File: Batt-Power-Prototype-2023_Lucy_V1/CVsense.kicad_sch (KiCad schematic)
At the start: 26 parts, among them U11 TSV912IDT, U5 ACS723xLCTR-10AU, U6 TSV912IDT, U8 TSV912IDT

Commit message: made changes to schematic
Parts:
- added C16 (x3): 100n, Capacitor_SMD:C_0603_1608Metric, symbol Device:C
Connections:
- net +5V: now also C16.1, C16.1, C16.1
- net GND: now also C16.2, C16.2, C16.2
- net Battery_Current renamed BAttery_Crrnt
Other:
- moved on the sheet: C16, U11C, U8C

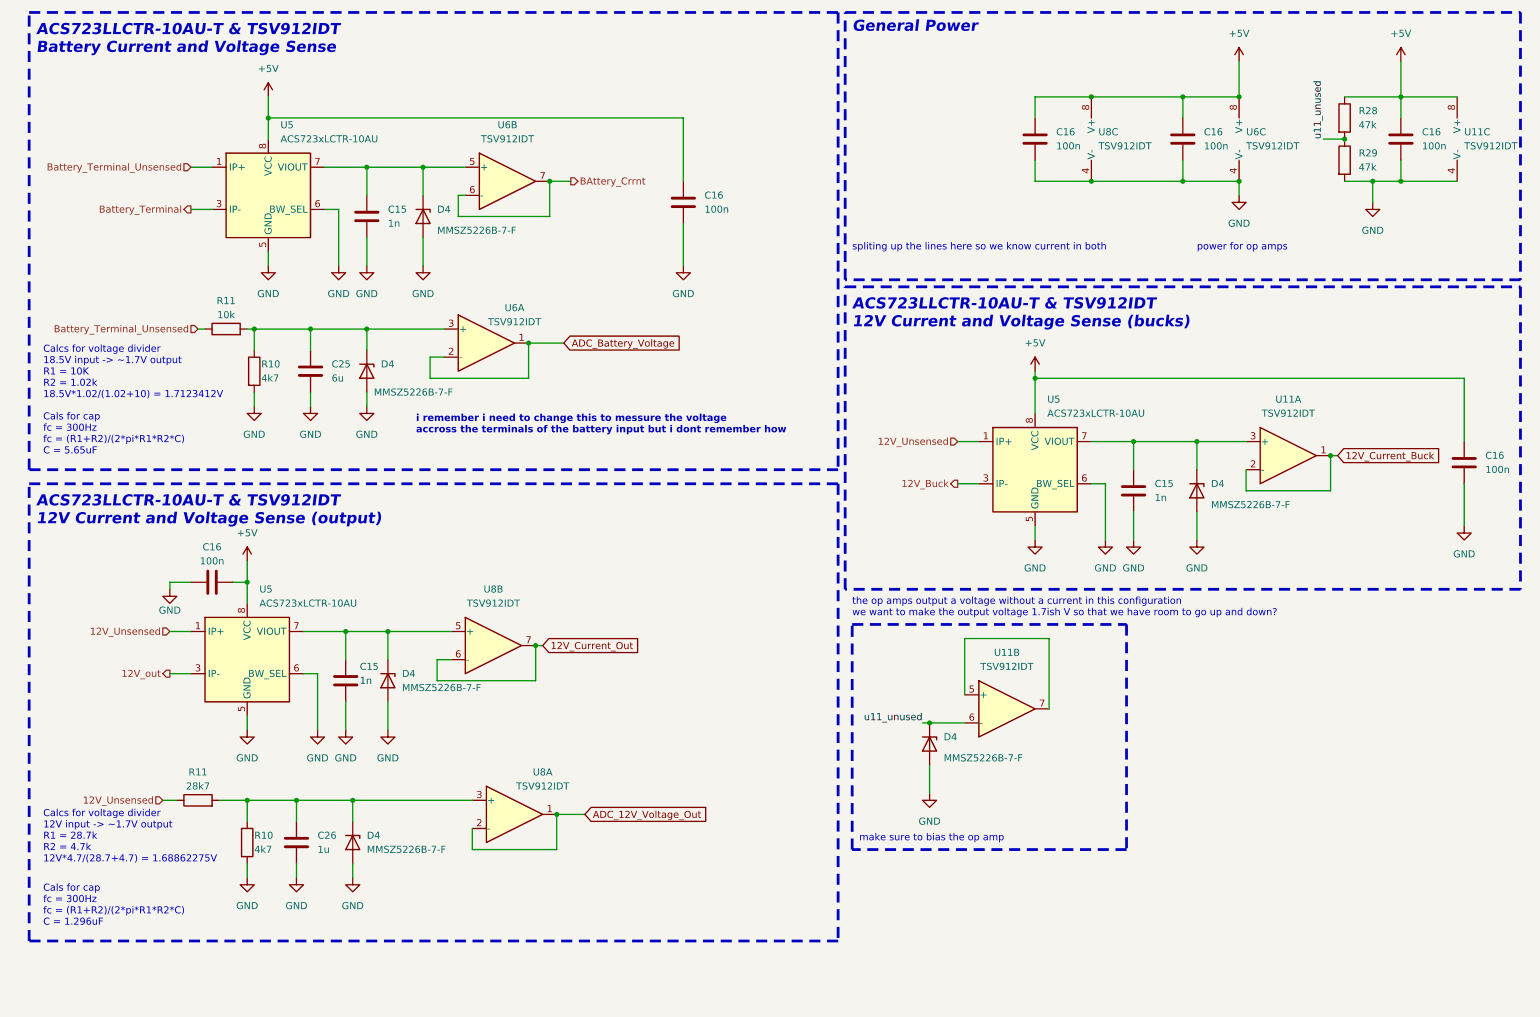
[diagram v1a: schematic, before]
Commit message: no more global variables
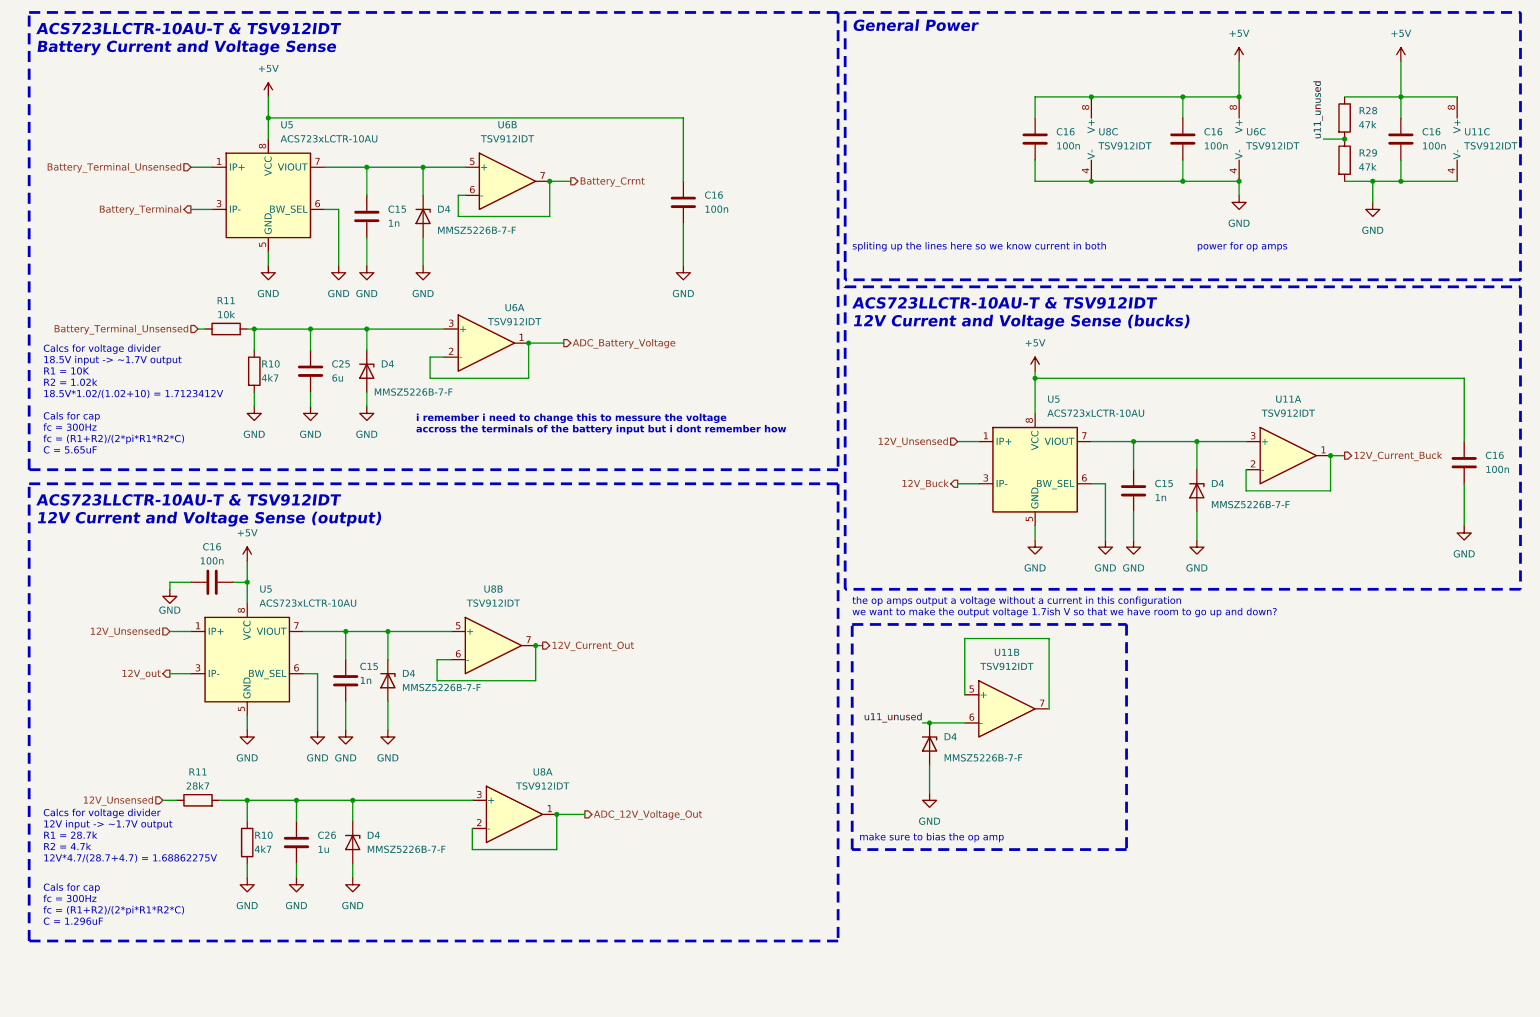
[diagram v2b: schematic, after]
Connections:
- net BAttery_Crrnt renamed Battery_Crrnt
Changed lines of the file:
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@@
     (stroke (width 0) (type default))
   )
-  (wire (pts (xy 248.92 93.98) (xy 250.19 93.98))
+  (wire (pts (xy 248.92 93.98) (xy 251.46 93.98))
     (stroke (width 0) (type default))
   )
@@
     (effects (font (size 1.27 1.27)) (justify right bottom))
   )
-  (global_label "12V_Current_Out" (shape input) (at 106.68 128.27 0) (fields_autoplaced)
-    (effects (font (size 1.27 1.27)) (justify left))
-    (property "Intersheetrefs" "${INTERSHEET_REFS}" (at 125.2679 128.27 0)
-      (effects (font (size 1.27 1.27)) (justify left) hide)
-    )
-  )
-  (global_label "12V_Current_Buck" (shape input) (at 250.19 93.98 0) (fields_autoplaced)
-    (effects (font (size 1.27 1.27)) (justify left))
-    (property "Intersheetrefs" "${INTERSHEET_REFS}" (at 270.1084 93.98 0)
-      (effects (font (size 1.27 1.27)) (justify left) hide)
-    )
-  )
-  (global_label "ADC_Battery_Voltage" (shape input) (at 110.49 73.66 0) (fields_autoplaced)
-    (effects (font (size 1.27 1.27)) (justify left))
-    (property "Intersheetrefs" "${INTERSHEET_REFS}" (at 132.7669 73.66 0)
-      (effects (font (size 1.27 1.27)) (justify left) hide)
-    )
-  )
-  (global_label "ADC_12V_Voltage_Out" (shape input) (at 114.3 158.75 0) (fields_autoplaced)
-    (effects (font (size 1.27 1.27)) (justify left))
-    (property "Intersheetrefs" "${INTERSHEET_REFS}" (at 137.5445 158.75 0)
-      (effects (font (size 1.27 1.27)) (justify left) hide)
-    )
-  )
   (hierarchical_label "Battery_Terminal_Unsensed" (shape input) (at 44.45 71.12 180) (fields_autoplaced)
     (effects (font (size 1.27 1.27)) (justify right))
@@
     (effects (font (size 1.27 1.27)) (justify right))
   )
+  (hierarchical_label "ADC_12V_Voltage_Out" (shape output) (at 114.3 158.75 0) (fields_autoplaced)
+    (effects (font (size 1.27 1.27)) (justify left))
+  )
+  (hierarchical_label "ADC_Battery_Voltage" (shape output) (at 110.49 73.66 0) (fields_autoplaced)
+    (effects (font (size 1.27 1.27)) (justify left))
+  )
   (hierarchical_label "12V_Unsensed" (shape input) (at 181.61 91.44 180) (fields_autoplaced)
     (effects (font (size 1.27 1.27)) (justify right))
@@
     (effects (font (size 1.27 1.27)) (justify right))
   )
-  (hierarchical_label "BAttery_Crrnt" (shape output) (at 111.76 44.45 0) (fields_autoplaced)
+  (hierarchical_label "Battery_Crrnt" (shape output) (at 111.76 44.45 0) (fields_autoplaced)
+    (effects (font (size 1.27 1.27)) (justify left))
+  )
+  (hierarchical_label "12V_Current_Out" (shape output) (at 106.68 128.27 0) (fields_autoplaced)
     (effects (font (size 1.27 1.27)) (justify left))
   )
@@
     (effects (font (size 1.27 1.27)) (justify right))
   )
+  (hierarchical_label "12V_Current_Buck" (shape output) (at 251.46 93.98 0) (fields_autoplaced)
+    (effects (font (size 1.27 1.27)) (justify left))
+  )
   (hierarchical_label "Battery_Terminal_Unsensed" (shape input) (at 43.18 41.91 180) (fields_autoplaced)

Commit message: some of the touch ups
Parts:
- removed C16 (x2): 100n, Capacitor_SMD:C_0603_1608Metric, symbol Device:C
- added C? (x2): 100n, Capacitor_SMD:C_0603_1608Metric, symbol Device:C
- renumbered C26 to C36, C25 to C37, C16 to C?, C15 to C?, D4 to D?, R28 to R29, R29 to R30, R10 to R?, R11 to R?, U6 to U13, U8 to U13, U6 to U14, U8 to U14, U11 to U15, U5 to U?
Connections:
- net +5V: now also C?.2, C?.2
- net GND: now also C?.1, C?.1
- net 12V_out renamed 12V_PCBs

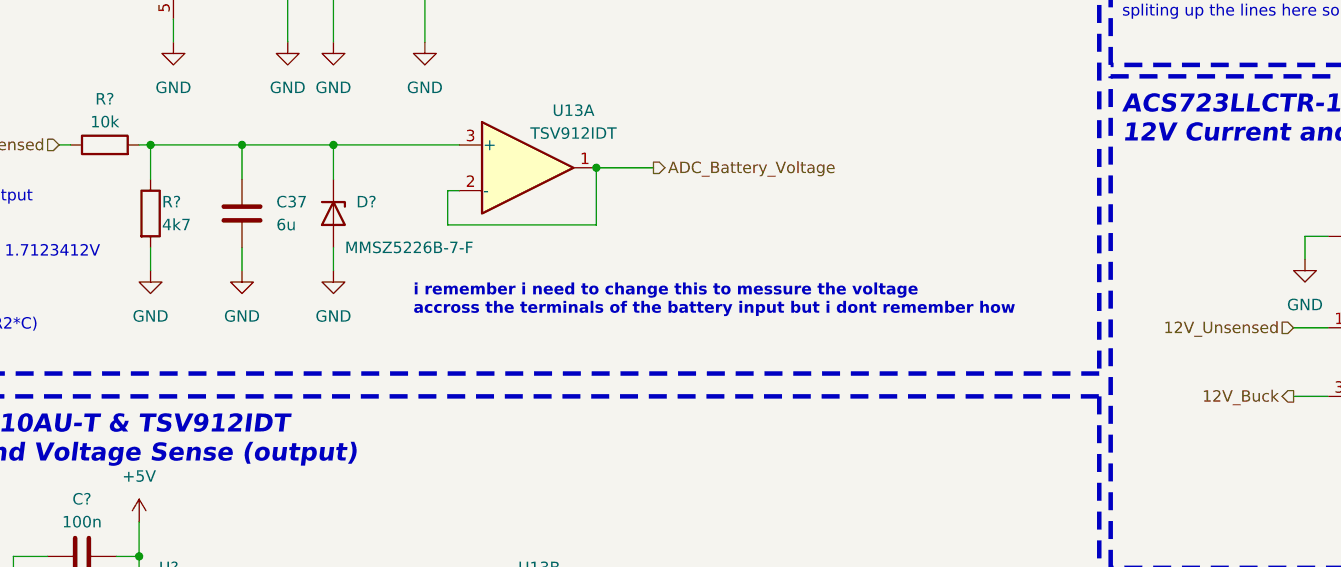
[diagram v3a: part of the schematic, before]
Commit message: everything but the battery input done
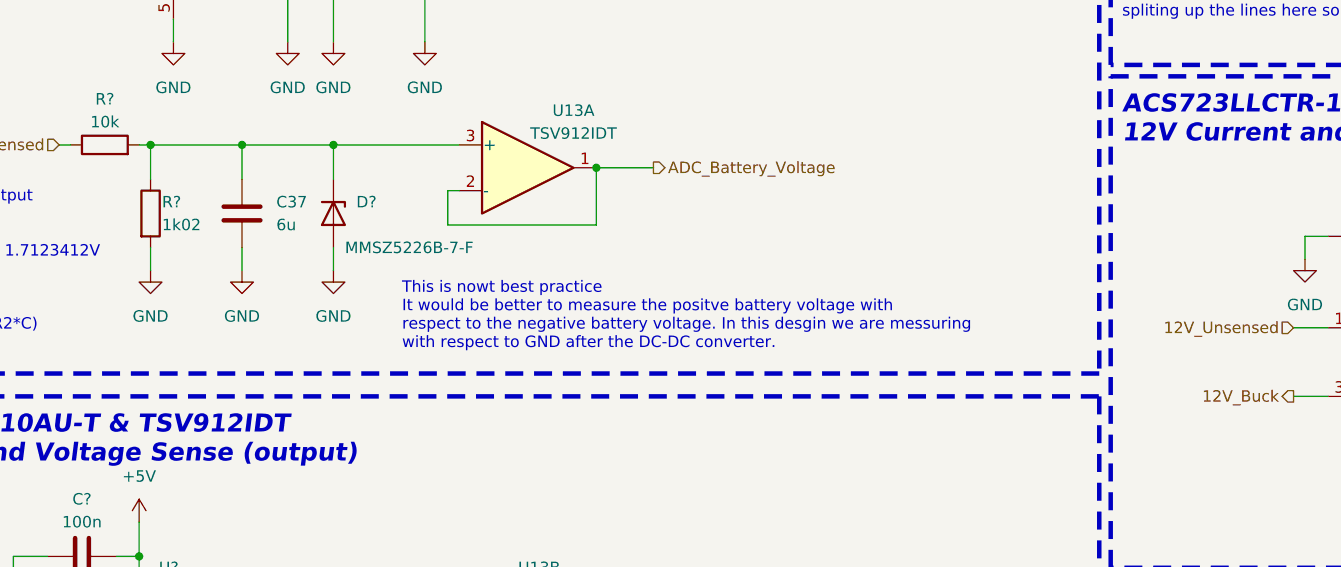
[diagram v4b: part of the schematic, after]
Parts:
- R?: value 4k7 -> 1k02
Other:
- note added: "This is nowt best practice It would be better to measure the positve battery voltage with respect to the negative battery voltage. In this desgin we are messuring with respect to GND after the DC-DC converter."
- note removed: "i remember i need to change this to messure the voltage accross the terminals of the battery input but i dont remember how"
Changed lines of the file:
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@@
     (effects (font (size 2 2) (thickness 0.254) bold italic) (justify left bottom))
+  )
+  (text "This is nowt best practice\nIt would be better to measure the positve battery voltage with \nrespect to the negative battery voltage. In this desgin we are messuring\nwith respect to GND after the DC-DC converter."
+    (at 82.55 93.98 0)
+    (effects (font (size 1.27 1.27)) (justify left bottom))
   )
   (text "Calcs for voltage divider\n18.5V input -> ~1.7V output\nR1 = 10K \nR2 = 1.02k\n18.5V*1.02/(1.02+10) = 1.7123412V"
@@
     (at 162.56 71.12 0)
     (effects (font (size 2 2) (thickness 0.254) bold italic) (justify left bottom))
-  )
-  (text "i remember i need to change this to messure the voltage \naccross the terminals of the battery input but i dont remember how"
-    (at 83.82 90.17 0)
-    (effects (font (size 1.27 1.27) (thickness 0.254) bold) (justify left bottom))
   )
   (text "spliting up the lines here so we know current in both\n"
@@
       (effects (font (size 1.27 1.27)) (justify left))
     )
-    (property "Value" "4k7" (at 55.88 80.01 0)
+    (property "Value" "1k02" (at 55.88 80.01 0)
       (effects (font (size 1.27 1.27)) (justify left))
     )

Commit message: everything
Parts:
- U13, U14, U15: Digikey # (none) -> 497-8165-2-ND
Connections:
- net 12V_Current_Out: now also U14.1, U14.2 (-); no longer U13.6 (-), U13.7
- net ADC_12V_Voltage_Out: now also U14.6 (-), U14.7; no longer U14.1, U14.2 (-)
- net ADC_Battery_Voltage: now also U13.6 (-), U13.7; no longer U13.1, U13.2 (-)
- net Battery_Crrnt: now also U13.1, U13.2 (-); no longer U14.6 (-), U14.7
- net at C37.1, D?.1 (K), R?.1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: now also U13.5 (+); no longer U13.3 (+)
- net at C?.1, D?.1 (K), U?.7 (VIOUT): now also U13.3 (+); no longer U14.5 (+)
- net at C?.1, D?.1 (K), U?.7 (VIOUT): now also U14.3 (+); no longer U13.5 (+)
- net at C36.1, D?.1 (K), R?.1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: now also U14.5 (+); no longer U14.3 (+)
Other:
- moved on the sheet: U13A, U13B, U14A, U14B

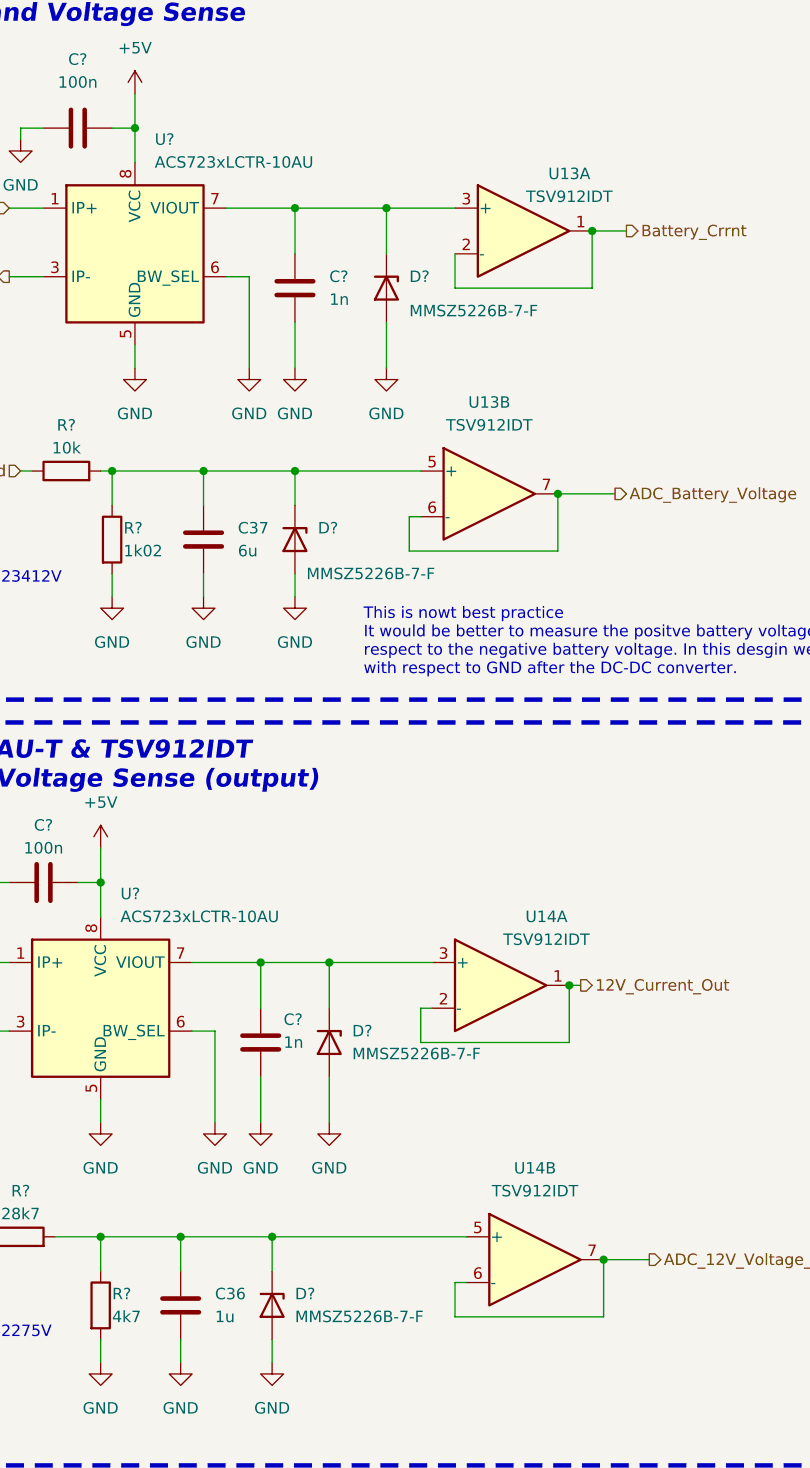
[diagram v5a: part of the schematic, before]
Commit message: Added bucks and fixed pinouts
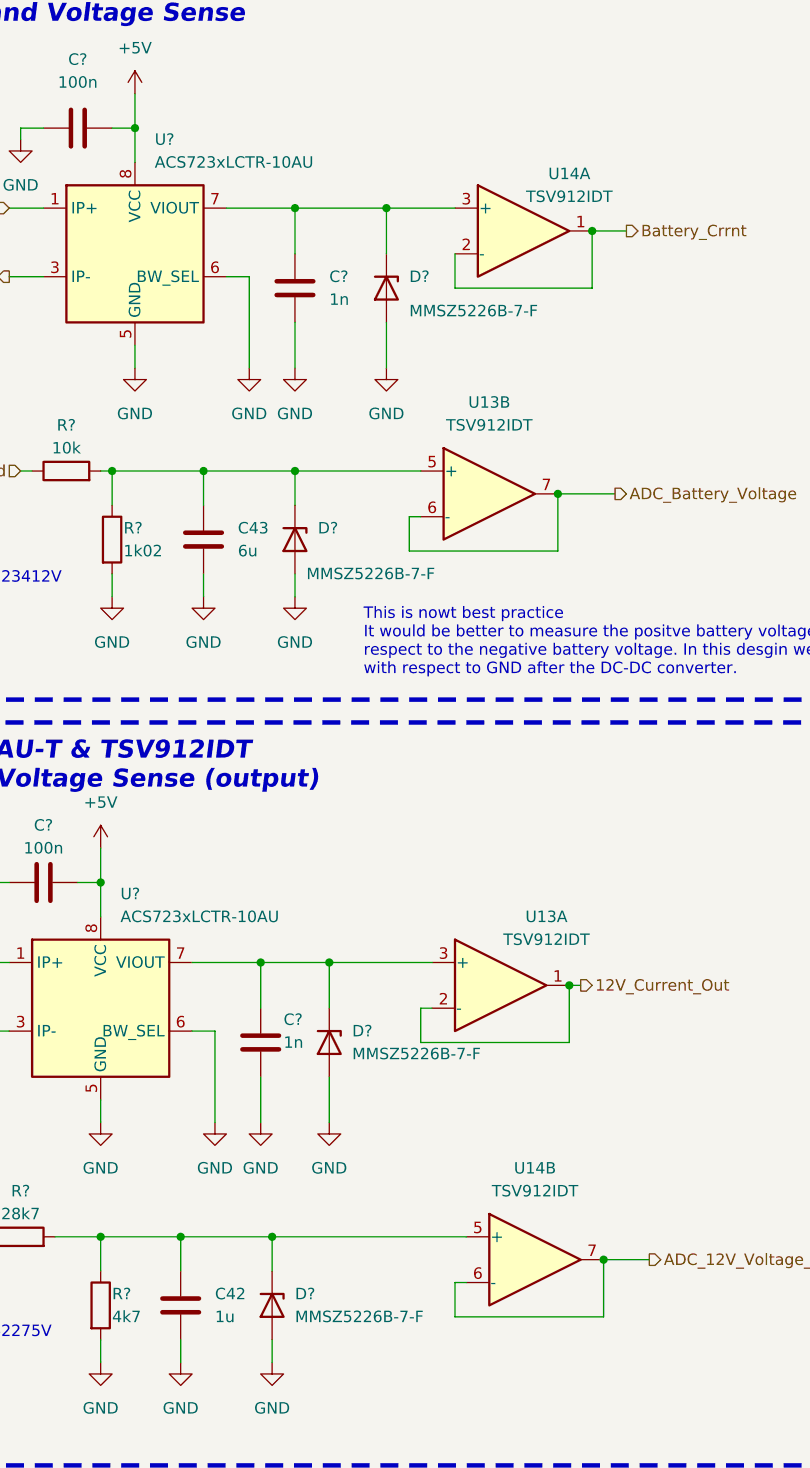
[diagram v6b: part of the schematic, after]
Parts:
- renumbered C36 to C42, C37 to C43, U14 to U13, U13 to U14
